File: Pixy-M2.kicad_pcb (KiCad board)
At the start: 4 copper layers, 66 x 100 mm, 78 parts, among them J1 USB_C_Receptacle_USB2.0_14P, J10 SM09B-SRSS-TB, J11 SM06B-SRSS-TB, J4 SM06B-SRSS-TB, J5 SM06B-SRSS-TB, J6 SM06B-SRSS-TB, J7 SM06B-SRSS-TB, J8 S6B-PH-K, J9 S6B-PH-K, Q1 AO4407A, SW1 SW_Push, SW2 SW_Push, SW3 JS102011SAQN, U1 ESP32-S3-WROOM-1-N16, U2 USBLC6-2SC6, U3 AP63203WU, U4 DRV8231ADSG, U5 DRV8231ADSG

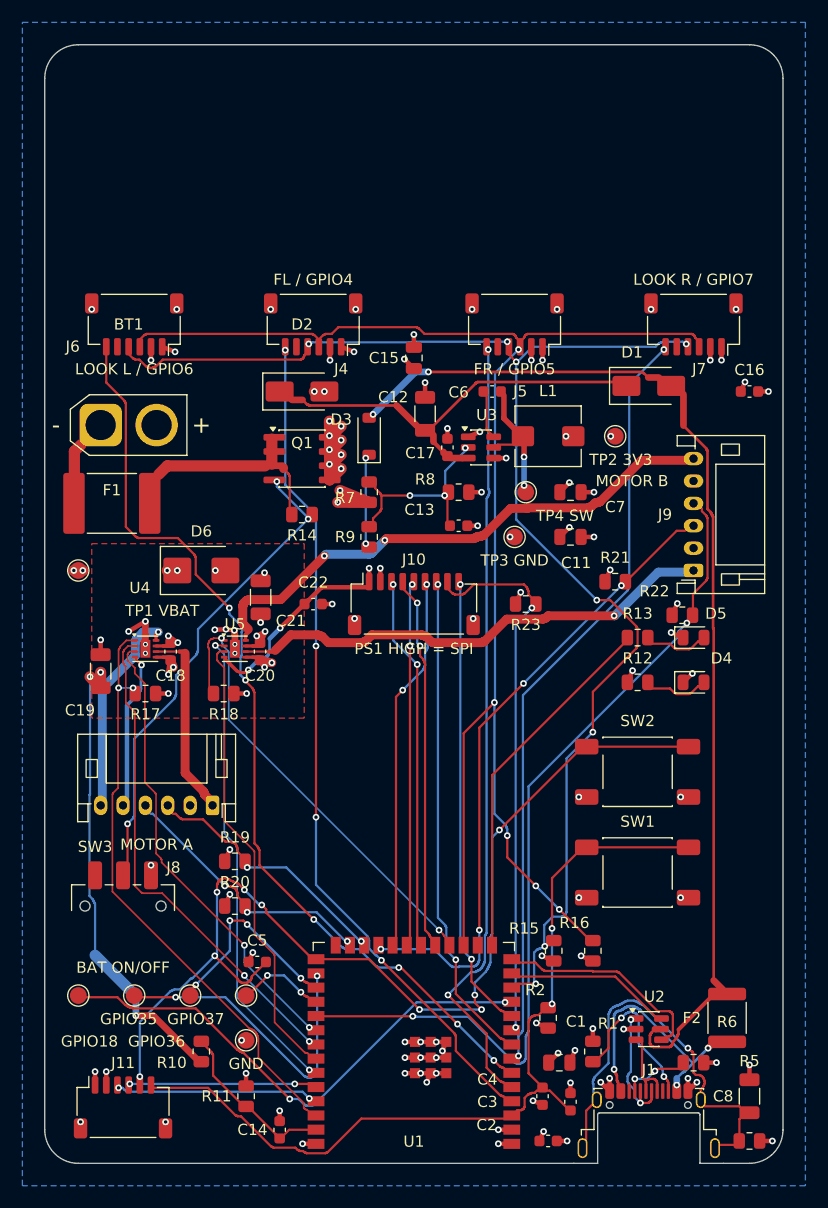
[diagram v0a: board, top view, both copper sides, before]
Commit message: layout: pair the motor-B outputs for review finding 4
MOT_B_1 ran at y ~ 113 while MOT_B_2 detoured through the regulator at
y ~ 97-105, so the two were 7.2 mm apart on average and the loop they enclose
was 423.6 mm2 as first routed (347.9 after the issue 1-3 pass, which widened
them but did not bring them together).

rework.py now routes MOT_B_1 first, samples its finished polyline, offsets each
sample 1.15 mm toward the side MOT_B_2 has to end up on, and routes MOT_B_2
through those points as waypoints; an unreachable waypoint is skipped rather
than failing the net.

                                first routed   after 1-3      now
  enclosed loop area              423.6 mm2    347.9 mm2    111.5 mm2
  pair separation mean / worst            -   7.17/9.65mm  1.39/5.27mm
  motor copper to REG_EN            0.27 mm      1.00 mm      8.51 mm
  motor copper to the SW node       0.28 mm      1.33 mm      6.62 mm
  motor copper to VSYS at U3        0.28 mm      5.52 mm      9.00 mm

U5 was deliberately not moved, which is the review's first suggestion. The In2
VBAT island stops at x=127 and J9 is at x=158, so a driver there would be off
the motor supply plane; the space west of J9 is the buck output (L1, C7, C11),
so it would put a switching driver hard against the regulator and undo the
clearances above; and it would split the motor region away from D6, the bulk
capacitance and the battery entry.

Two costs, both measured:

  MOT_B_2 is 6.4 mm longer (48.6 -> 55.0 mm), so the pair's resistance goes
  61.5 -> 65.4 mOhm: +5.7 mV and +8 mW at the 1.47 A limit.

  Motor copper within 0.6 mm of the BNO08x SPI nets doubles, 5.0 -> 11.0 mm,
  because the shared corridor passes under J10's fan-out. That is ~13 separate
  encounters of 0.2-2.0 mm - crossings, not a parallel run - and the longest is
  against GPIO16, the module's RST line with a 10k pull-up, not a clock or data
  line. Taken deliberately: coupling into REG_EN trips a comparator and stops
  the robot, while a dis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
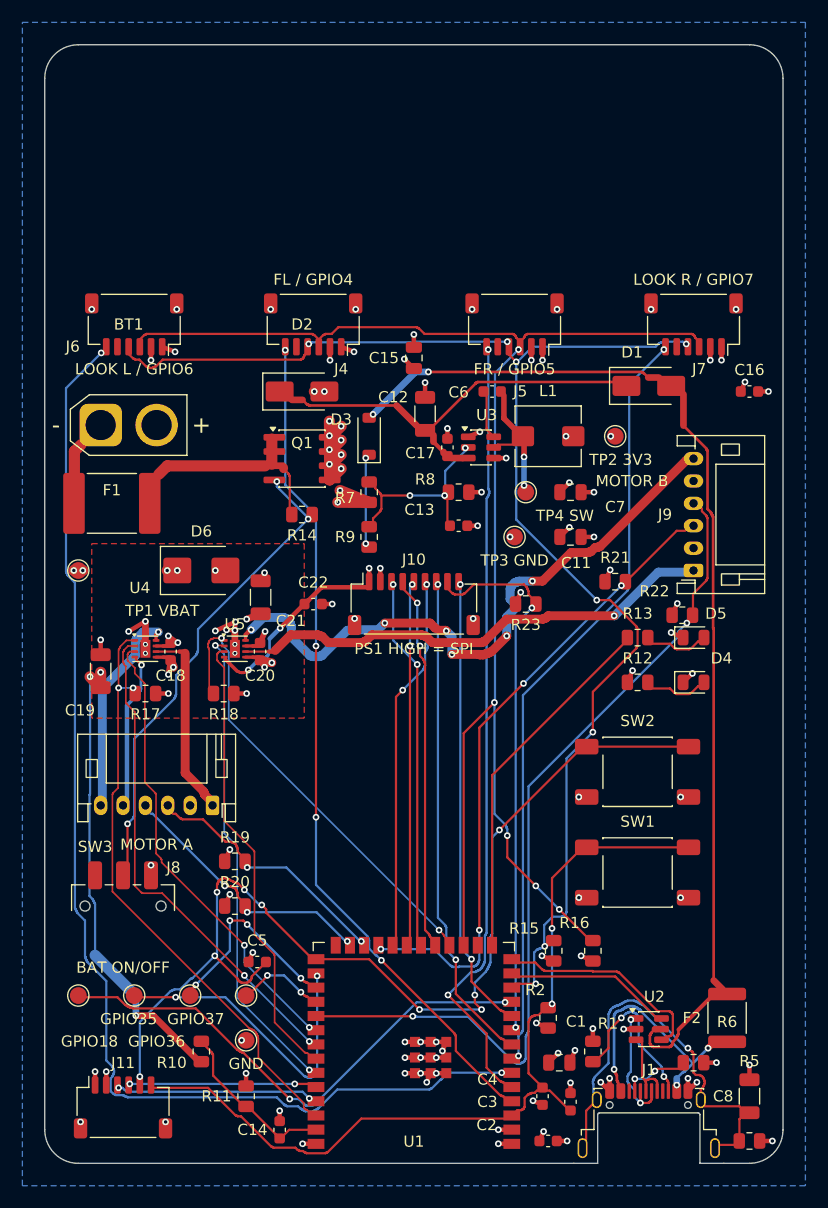
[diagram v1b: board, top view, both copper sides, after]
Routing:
- net /GPIO6: track 83.2 -> 107.1 mm, vias 6 -> 2
- net /MOT_B_2: track 48.6 -> 55.0 mm, vias 2 -> 6
- net GND: track 78.4 -> 79.3 mm
- net /VBAT: track 68.2 -> 68.8 mm

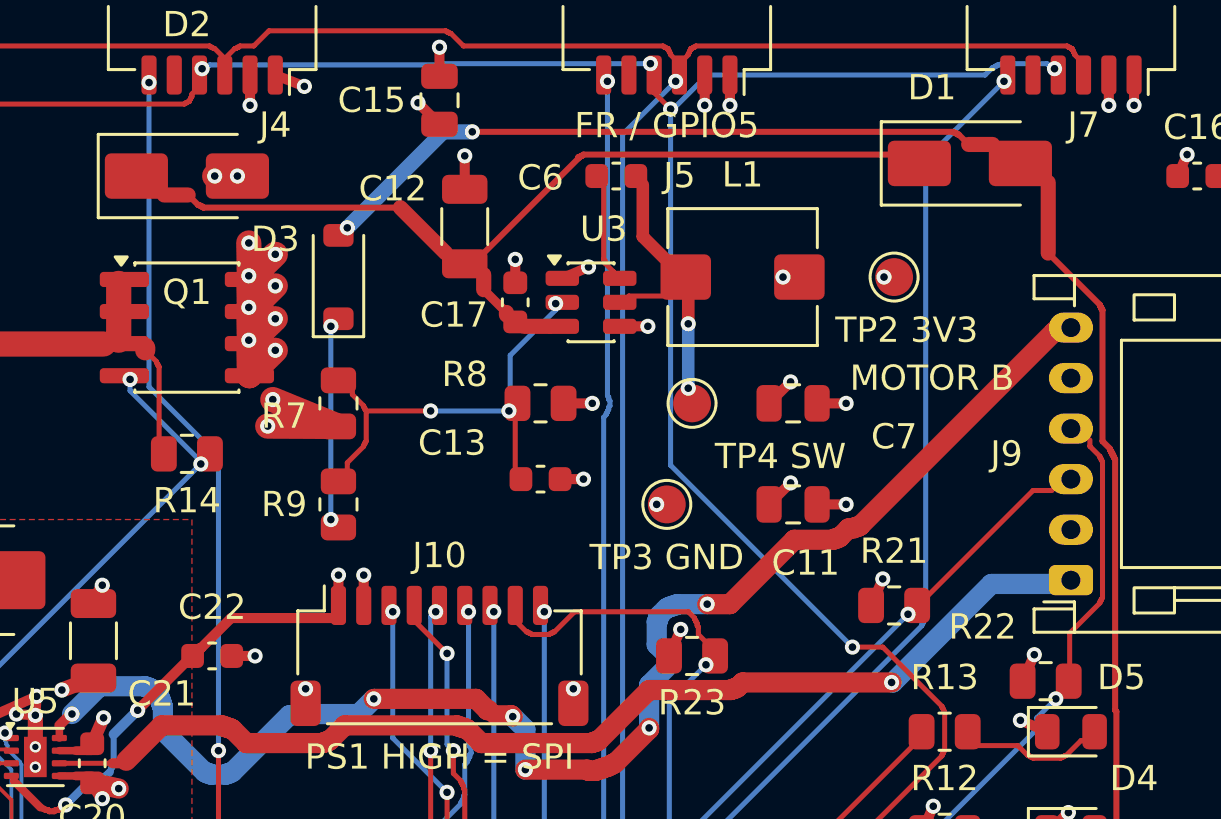
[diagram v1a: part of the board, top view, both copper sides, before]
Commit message: layout: rework the buck power stage for review finding 5
Four complaints, all about the regulator block being spread out rather than
wrong. Six parts moved and the block hand routed in rework.py's buck_block().

                                    before        after
  SW node copper area              5.17 mm2     3.57 mm2
  SW node on B.Cu                  2.55 mm      0 mm
  SW node vias                     2            0
  C6 (BST) pad to U3.6             4.15 mm      2.25 mm
  U3.4 return via to C17's         5.88 mm      0.95 mm
  L1.2 to C11.1 through copper     none         6.95 mm on F.Cu
  C7.1 to C11.1                    4.00 mm      2.30 mm
  FB / 3V3 copper to SW or BST     0.27 mm      2.10 mm
  VSYS copper to SW or BST         0.83 mm      2.07 mm

Moved: C6 (140,91)->(139.5,93.3), C17 (136,96) rot90 ->(139,98.6) rot0,
C7 (147,100)->(147,99), C11 (147,104)->(147,101.3), R8 (137,100)->(136.6,100.6),
TP4 (143,100)->(141.9,99.6).

U3 is a TSOT-23-6 with IN (pin 3) and GND (pin 4) at the same y on opposite
sides, so the input capacitor goes underneath spanning the two - the tightest
loop this pinout allows. TP4's two vias and back-layer branch are gone, replaced
by one 3.2 mm top stub to a pad that is still clear of the inductor body. L1 ->
C7 -> C11 is now a single 0.8 mm top-layer run; before, all three tapped the In2
pour independently and no copper joined them at all, which loop.py confirms by
finding no path between them on the old board. FB left its via 1.2 mm from BST
and became a dedicated 0.2 mm sense trace to C11, the far output capacitor.

The bootstrap capacitor could not go where it belongs. BST and SW are adjacent
pins, so the ideal is a vertical 0603 straddling them, but L1's courtyard starts
0.45 mm past U3's. C6 went above the package instead, which halves the BST run
rather than perfecting it. Moving L1 east would buy the ideal placement at the
cost of a longer switch node - the wrong trade, since the node is the primary
radiator and the 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
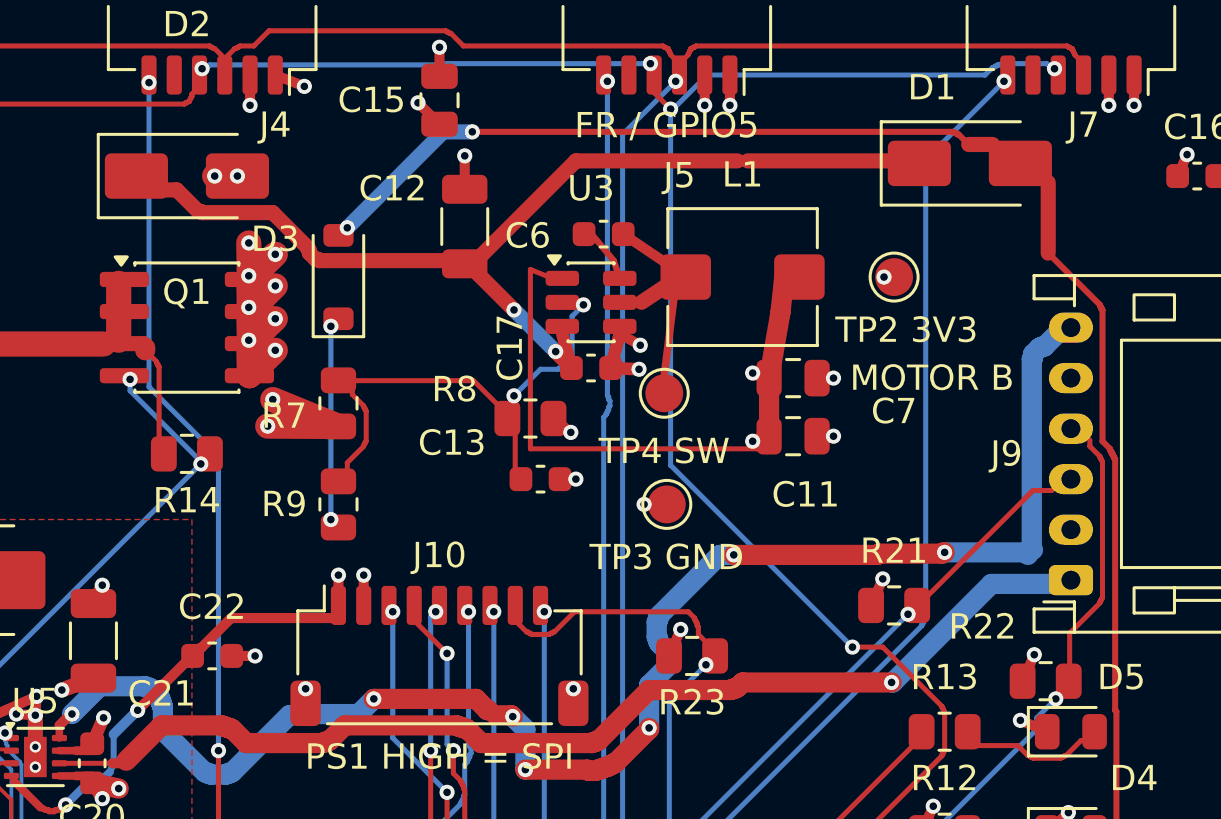
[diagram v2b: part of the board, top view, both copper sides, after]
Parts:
- moved C17 3.97 mm to (139.0, 98.6), turned to 0 degrees
- moved C11 2.70 mm to (147.0, 101.3)
- moved C6 2.35 mm to (139.5, 93.3)
- moved TP4 1.17 mm to (141.9, 99.6)
- moved C7 1.00 mm to (147.0, 99.0)
- moved R8 0.72 mm to (136.6, 100.6)
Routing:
- net /ESP_3V3: track 57.9 -> 79.1 mm, vias 28 -> 26
- net /MOT_B_2: track 55.0 -> 59.4 mm, vias 6 -> 7
- net /VSYS: track 32.9 -> 37.2 mm, vias 0 -> 2
- net Net-(U3-BST): track 3.72 -> 2.11 mm
- net /REG_EN: track 16.4 -> 17.4 mm, vias 3 -> 2
- net Net-(U3-SW): track 8.44 -> 7.85 mm, vias 2 -> 0

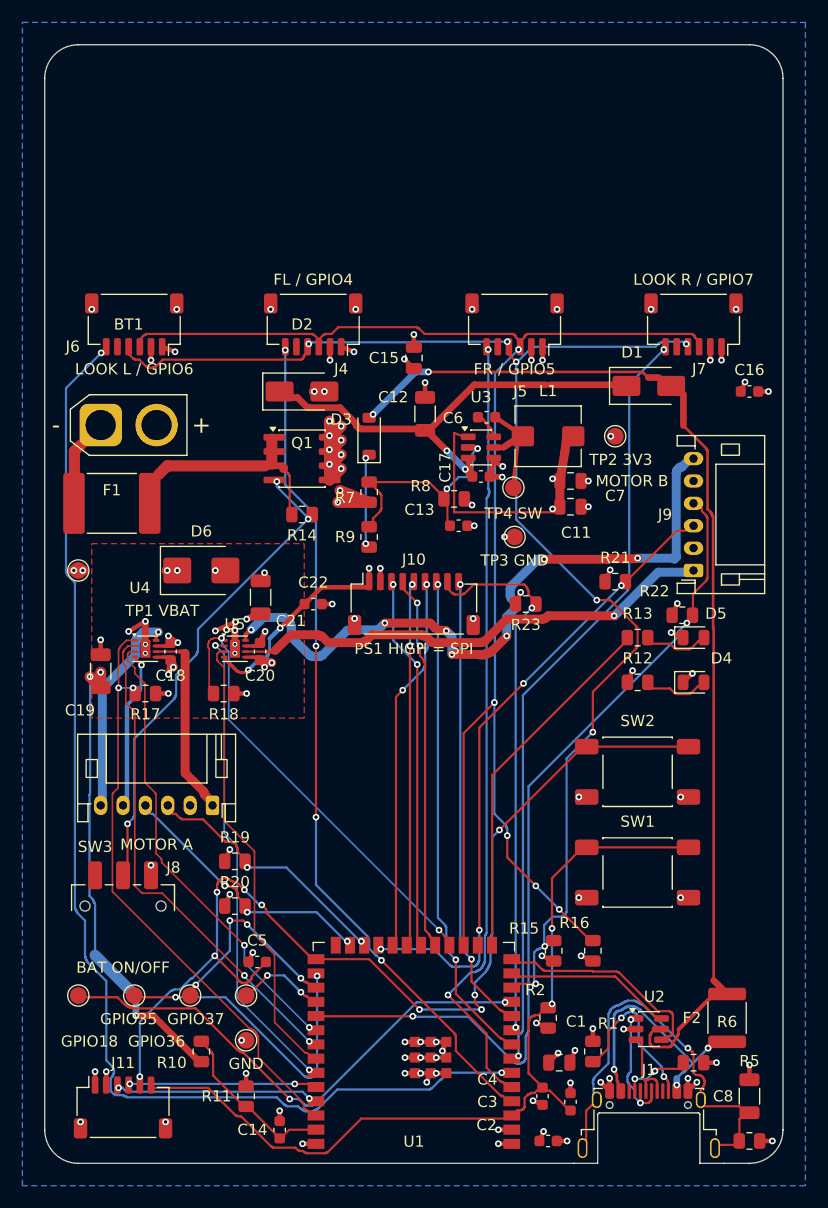
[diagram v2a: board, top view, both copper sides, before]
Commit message: layout: get vias out of pad openings for review finding 6
73 vias sat inside a pad's solder-mask opening, 65 of them under solder paste.
That is the original router's doing: wire.py deliberately drops stitching vias
into pads 1.2 mm and larger, and its A* via search never excluded pads at all.

                                      before    after
  vias inside a pad opening             73        4
  ...of those, under solder paste       65        0
  board track                     2313.8 mm  2431.8 mm
  vias                                 247      247

The four that remain are the U4/U5 exposed-pad thermal vias from finding 2,
which are in a pad on purpose. Everything else moved out two ways:

  54 stepped out of their pad and left a 0.25 mm stub behind on F.Cu, plus one
  on B.Cu where a back-layer track ended at the old position. The constraint is
  the mask opening, not the copper - via and pad are the same net, so copper
  overlap is harmless and only the drill needs the margin.

  15 had nowhere to step to (U1's castellations, the 0.6 mm JST-SH pads on
  J4/J5/J7/J10/J11, U2, R20, R23), so their 11 nets were ripped and routed
  again. rework.py's via search already refuses to land in a pad, so the
  replacement route simply does not need a via there. All 11 re-routed.

The four vias in test-point pads moved too, although those pads take no paste
and so were never a wicking risk. Moving them makes the rule on this board one
sentence that is cheap to re-check: no via lies in a pad opening except the four
thermal vias, and those carry a fabrication note.

KiCad cannot express the via-in-pad requirement per via. A via accepts
(covering ...), (plugging ...) and (tenting ...), but filling and capping are
board-wide settings only - verified by trying each form against kicad-cli.
Turning them on globally would change the process and the price for all 247
vias, which is an ordering decision rather than a layout one, so the requirement
goes on Dwgs.User instead: the f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
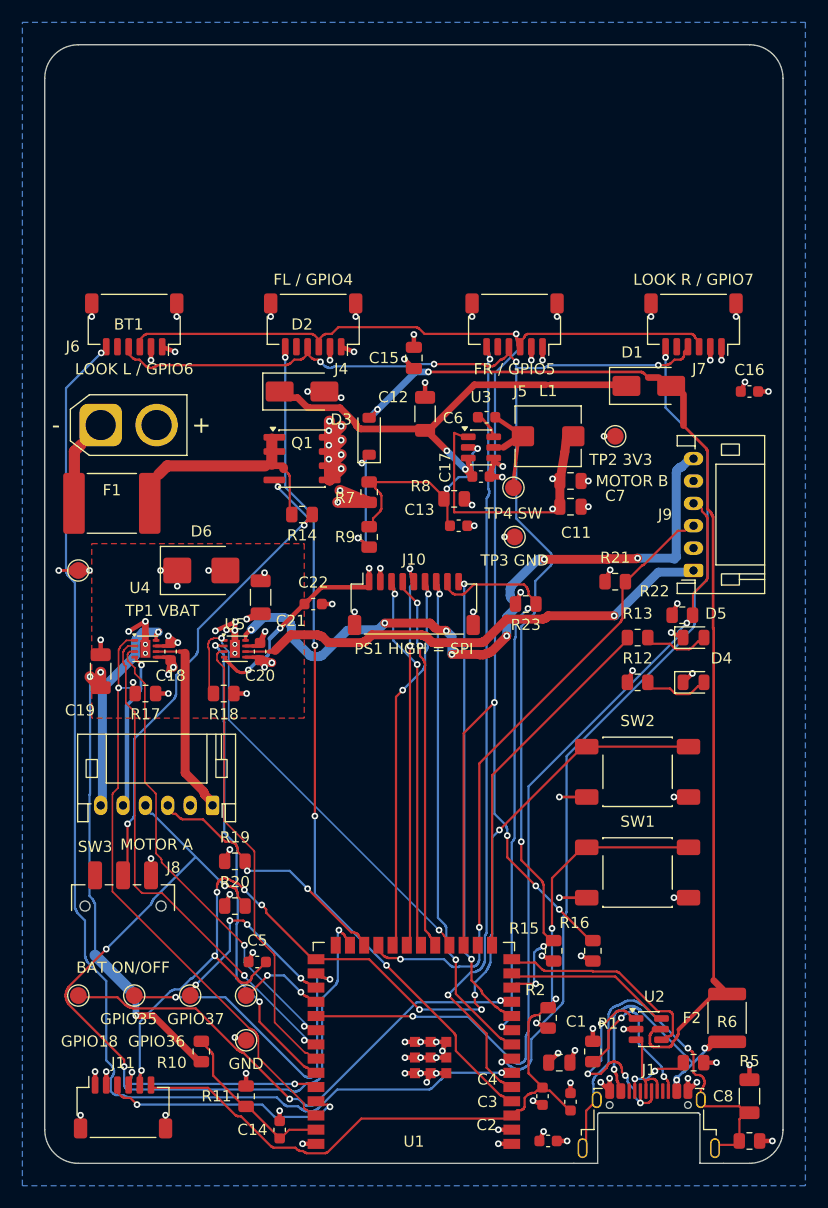
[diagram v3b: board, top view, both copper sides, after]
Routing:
- net /GPIO48: track 21.6 -> 72.4 mm, vias 3 -> 4
- net GND: track 79.6 -> 93.8 mm
- net Net-(J1-D--PadA7): track 9.83 -> 17.9 mm, vias 2 -> 4
- net /VBAT: track 68.8 -> 76.3 mm
- net /GPIO7: track 68.5 -> 74.9 mm
- net /GPIO8: track 119.4 -> 114.3 mm, vias 8 -> 7
- net /GPIO43: track 17.4 -> 21.1 mm
- net Net-(D3-K): track 7.65 -> 10.5 mm
- net /GPIO9: track 130.6 -> 133.4 mm
- net /GPIO13: track 31.7 -> 34.6 mm
- net /GPIO35: track 27.6 -> 30.0 mm
- net Net-(Q1-G): track 41.8 -> 44.1 mm
- net /GPIO44: track 16.1 -> 18.2 mm
- net /GPIO15: track 43.4 -> 45.1 mm
- net /GPIO5: track 69.8 -> 71.5 mm
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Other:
- board text added: "(IPC-4761 type VII). Confirm the option with the fabricator: tenting and"
- board text added: "FAB NOTE - VIA IN PAD"
- board text added: "The four 0.25 mm vias inside the U4 and U5 exposed pads (DRV8231A) are"
- board text added: "board lies inside a pad opening."
- board text added: "filled/capped via-in-pad are different processes. No other via on this"
- board text added: "thermal vias and sit under solder paste. They require resin fill and cap"
